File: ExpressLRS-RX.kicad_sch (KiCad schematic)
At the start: 34 parts, among them J2 Conn_Coaxial, U60 ESP8285H16, U61 Crystal_GND24, U70 SX1280, U71 Crystal_GND24

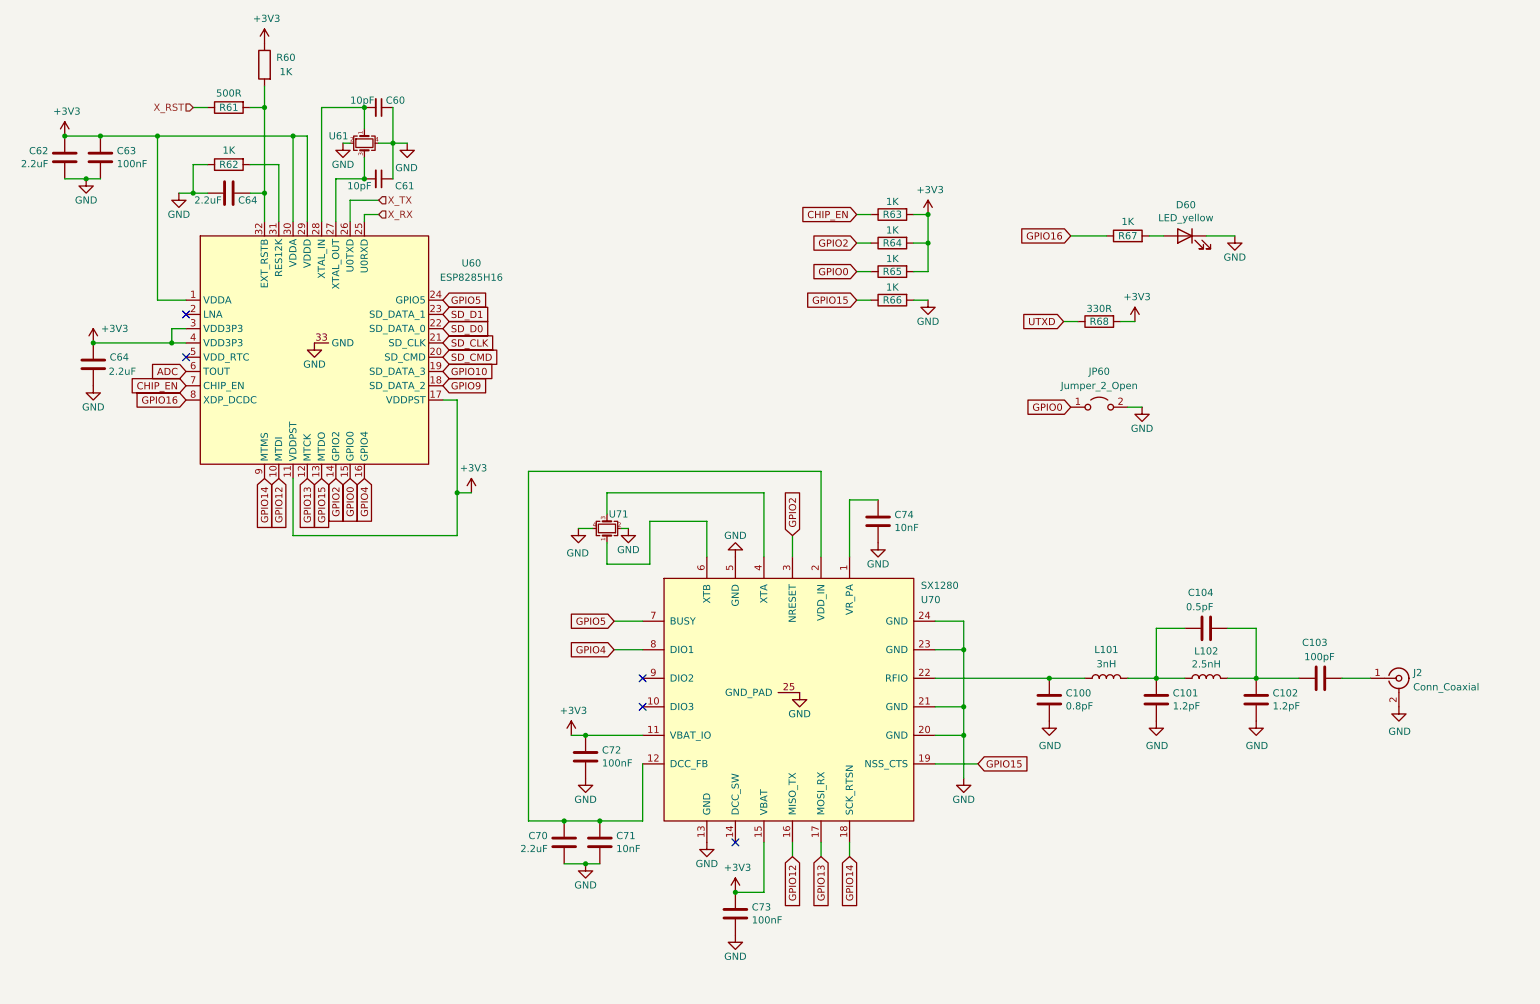
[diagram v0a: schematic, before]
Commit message: Initial board layout completed + initial routing started
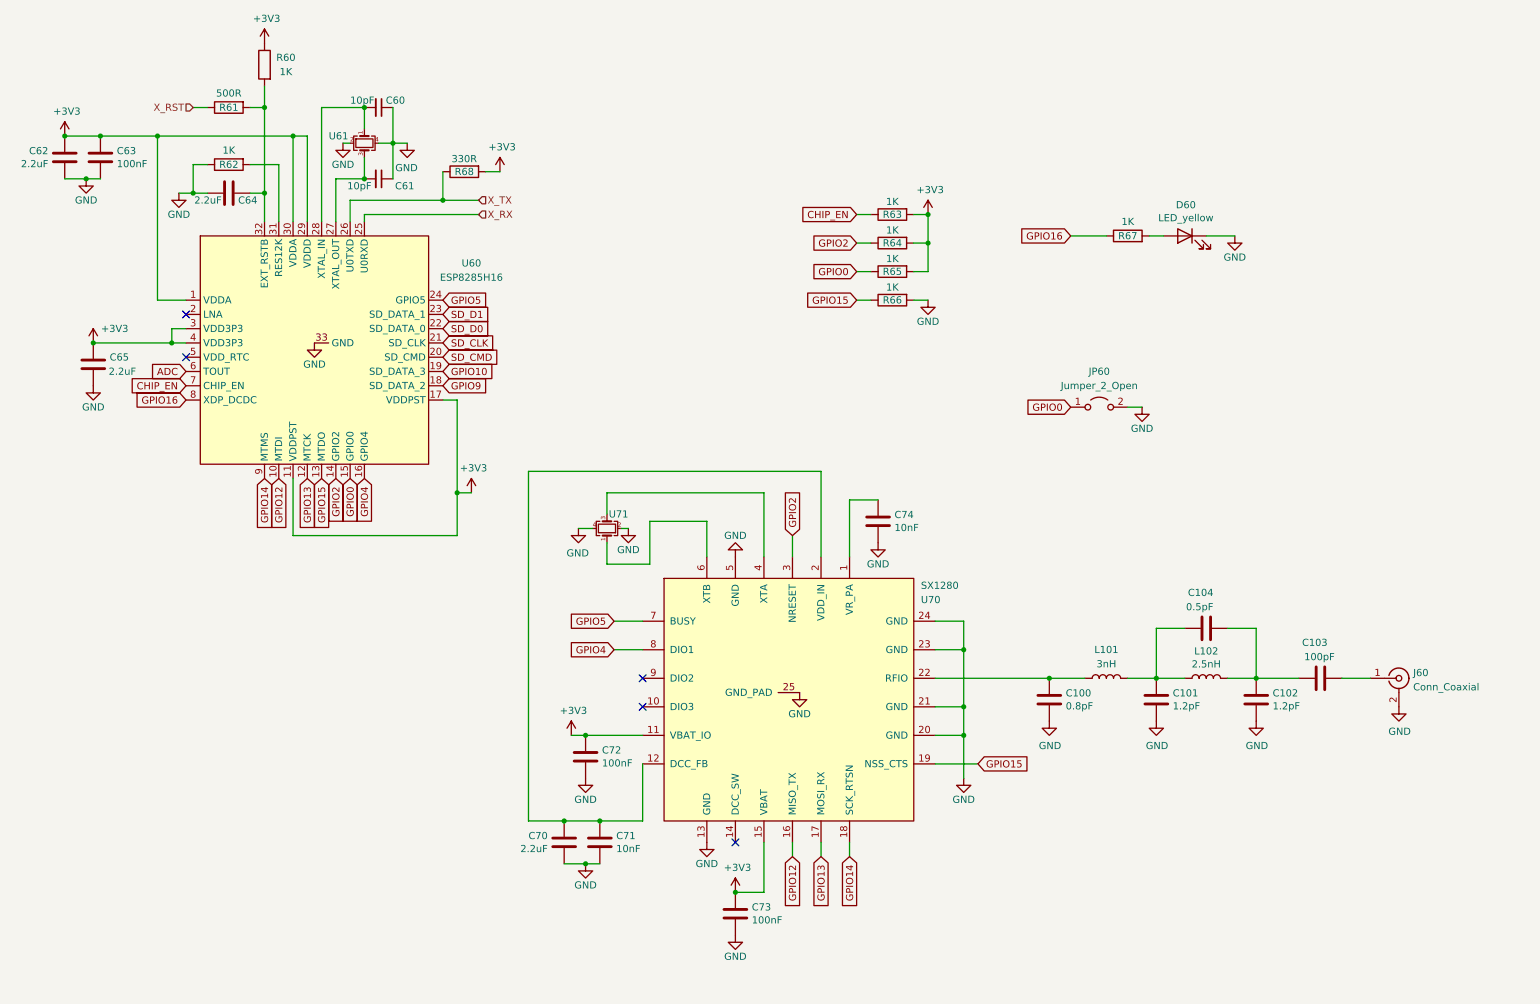
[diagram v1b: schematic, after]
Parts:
- U61: value Crystal_GND24 -> Crystal_ESP8285; footprint Crystal:Crystal_SMD_3225-4Pin_3.2x2.5mm -> Crystal:Crystal_SMD_2016-4Pin_2.0x1.6mm; LCSC C15192 -> C669081
- U71: value Crystal_GND24 -> Crystal_SX1280
- renumbered C64 to C65, J2 to J60
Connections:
- net UTXD is gone; now on net X_TX: R68.1
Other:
- moved on the sheet: R68
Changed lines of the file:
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@@
   (junction (at 143.51 173.99) (diameter 0) (color 0 0 0 0)
+  )
+  (junction (at 91.44 50.8) (diameter 0) (color 0 0 0 0)
   )
   (junction (at 77.47 46.99) (diameter 0) (color 0 0 0 0)
@@
     (stroke (width 0) (type default) (color 0 0 0 0))
   )
+  (wire (pts (xy 91.44 45.72) (xy 91.44 50.8))
+    (stroke (width 0) (type default) (color 0 0 0 0))
+  )
   (wire (pts (xy 106.68 161.29) (xy 113.03 161.29))
     (stroke (width 0) (type default) (color 0 0 0 0))
@@
     (stroke (width 0) (type default) (color 0 0 0 0))
   )
-  (wire (pts (xy 80.01 50.8) (xy 74.93 50.8))
+  (wire (pts (xy 97.79 50.8) (xy 91.44 50.8))
     (stroke (width 0) (type default) (color 0 0 0 0))
   )
@@
     (stroke (width 0) (type default) (color 0 0 0 0))
   )
-  (wire (pts (xy 212.09 72.39) (xy 214.63 72.39))
+  (wire (pts (xy 99.06 45.72) (xy 101.6 45.72))
     (stroke (width 0) (type default) (color 0 0 0 0))
   )
@@
     (stroke (width 0) (type default) (color 0 0 0 0))
   )
-  (wire (pts (xy 201.93 72.39) (xy 204.47 72.39))
-    (stroke (width 0) (type default) (color 0 0 0 0))
-  )
   (wire (pts (xy 106.68 161.29) (xy 106.68 99.06))
     (stroke (width 0) (type default) (color 0 0 0 0))
@@
     (stroke (width 0) (type default) (color 0 0 0 0))
   )
-  (wire (pts (xy 77.47 53.34) (xy 80.01 53.34))
+  (wire (pts (xy 77.47 53.34) (xy 97.79 53.34))
     (stroke (width 0) (type default) (color 0 0 0 0))
   )
@@
     (stroke (width 0) (type default) (color 0 0 0 0))
   )
+  (wire (pts (xy 91.44 50.8) (xy 74.93 50.8))
+    (stroke (width 0) (type default) (color 0 0 0 0))
+  )
   (wire (pts (xy 184.15 140.97) (xy 184.15 130.81))
     (stroke (width 0) (type default) (color 0 0 0 0))
@@
     (effects (font (size 1.27 1.27)) (justify right))
     (property "Intersheet References" "${INTERSHEET_REFS}" (id 0) (at 113.911 125.8094 0)
-      (effects (font (size 1.27 1.27)) (justify right) hide)
-    )
-  )
-  (global_label "UTXD" (shape input) (at 201.93 72.39 180) (fields_autoplaced)
-    (effects (font (size 1.27 1.27)) (justify right))
-    (property "Intersheet References" "${INTERSHEET_REFS}" (id 0) (at 194.8282 72.4694 0)
       (effects (font (size 1.27 1.27)) (justify right) hide)
     )
@@
     )
   )
-  (hierarchical_label "X_TX" (shape input) (at 80.01 50.8 0)
+  (hierarchical_label "X_TX" (shape input) (at 97.79 50.8 0)
     (effects (font (size 1.27 1.27)) (justify left))
   )
-  (hierarchical_label "X_RX" (shape input) (at 80.01 53.34 0)
+  (hierarchical_label "X_RX" (shape input) (at 97.79 53.34 0)
     (effects (font (size 1.27 1.27)) (justify left))
   )
@@
   (symbol (lib_id "power:GND") (at 73.66 40.64 0) (unit 1)
     (in_bom yes) (on_board yes)
-    (property "Reference" "#PWR0111" (id 0) (at 73.66 46.99 0)
+    (property "Reference" "#PWR0165" (id 0) (at 73.66 46.99 0)
       (effects (font (size 1.27 1.27)) hide)
     )
@@
   (symbol (lib_id "power:GND") (at 261.62 140.97 0) (unit 1)
     (in_bom yes) (on_board yes)
-    (property "Reference" "#PWR0126" (id 0) (at 261.62 147.32 0)
+    (property "Reference" "#PWR0169" (id 0) (at 261.62 147.32 0)
       (effects (font (size 1.27 1.27)) hide)
     )
@@
   (symbol (lib_id "power:GND") (at 68.58 76.2 0) (unit 1)
     (in_bom yes) (on_board yes)
-    (property "Reference" "#PWR0110" (id 0) (at 68.58 82.55 0)
+    (property "Reference" "#PWR0167" (id 0) (at 68.58 82.55 0)
       (effects (font (size 1.27 1.27)) hide)
     )
@@
     (pin "1")
   )
-  (symbol (lib_id "Device:R") (at 208.28 72.39 90) (mirror x) (unit 1)
-    (in_bom yes) (on_board yes)
-    (property "Reference" "R68" (id 0) (at 208.28 72.39 90))
-    (property "Value" "330R" (id 1) (at 208.28 70.104 90))
-    (property "Footprint" "Resistor_SMD:R_0402_1005Metric" (id 2) (at 208.28 70.612 90)
-      (effects (font (size 1.27 1.27)) hide)
-    )
-    (property "Datasheet" "?" (id 3) (at 208.28 72.39 0)
-      (effects (font (size 1.27 1.27)) hide)
-    )
-    (property "LCSC" "?" (id 4) (at 208.28 72.39 0)
+  (symbol (lib_id "Device:R") (at 95.25 45.72 90) (mirror x) (unit 1)
+    (in_bom yes) (on_board yes)
+    (property "Reference" "R68" (id 0) (at 95.25 45.72 90))
+    (property "Value" "330R" (id 1) (at 95.25 43.434 90))
+    (property "Footprint" "Resistor_SMD:R_0402_1005Metric" (id 2) (at 95.25 43.942 90)
+      (effects (font (size 1.27 1.27)) hide)
+    )
+    (property "Datasheet" "?" (id 3) (at 95.25 45.72 0)
+      (effects (font (size 1.27 1.27)) hide)
+    )
+    (property "LCSC" "?" (id 4) (at 95.25 45.72 0)
       (effects (font (size 1.27 1.27)) hide)
     )
@@
   (symbol (lib_id "power:+3V3") (at 29.21 76.2 0) (unit 1)
     (in_bom yes) (on_board yes)
-    (property "Reference" "#PWR0107" (id 0) (at 29.21 80.01 0)
+    (property "Reference" "#PWR0166" (id 0) (at 29.21 80.01 0)
       (effects (font (size 1.27 1.27)) hide)
     )
@@
   (symbol (lib_id "power:+3V3") (at 177.8 53.34 0) (unit 1)
     (in_bom yes) (on_board yes)
-    (property "Reference" "#PWR0103" (id 0) (at 177.8 57.15 0)
+    (property "Reference" "#PWR0168" (id 0) (at 177.8 57.15 0)
       (effects (font (size 1.27 1.27)) hide)
     )
@@
   (symbol (lib_id "Device:C") (at 29.21 80.01 0) (mirror y) (unit 1)
     (in_bom yes) (on_board yes)
-    (property "Reference" "C64" (id 0) (at 35.56 78.74 0)
+    (property "Reference" "C65" (id 0) (at 35.56 78.74 0)
       (effects (font (size 1.27 1.27)) (justify left))
     )
@@
   (symbol (lib_id "Connector:Conn_Coaxial") (at 261.62 135.89 0) (unit 1)
     (in_bom yes) (on_board yes) (fields_autoplaced)
-    (property "Reference" "J2" (id 0) (at 264.16 134.9131 0)
+    (property "Reference" "J60" (id 0) (at 264.16 134.9131 0)
       (effects (font (size 1.27 1.27)) (justify left))
     )
@@
     (pin "1")
   )
-  (symbol (lib_id "power:+3V3") (at 214.63 72.39 0) (unit 1)
-    (in_bom yes) (on_board yes)
-    (property "Reference" "#PWR0115" (id 0) (at 214.63 76.2 0)
-      (effects (font (size 1.27 1.27)) hide)
-    )
-    (property "Value" "+3V3" (id 1) (at 215.011 67.9958 0))
-    (property "Footprint" "" (id 2) (at 214.63 72.39 0)
-      (effects (font (size 1.27 1.27)) hide)
-    )
-    (property "Datasheet" "" (id 3) (at 214.63 72.39 0)
+  (symbol (lib_id "power:+3V3") (at 101.6 45.72 0) (unit 1)
+    (in_bom yes) (on_board yes)
+    (property "Reference" "#PWR0115" (id 0) (at 101.6 49.53 0)
+      (effects (font (size 1.27 1.27)) hide)
+    )
+    (property "Value" "+3V3" (id 1) (at 101.981 41.3258 0))
+    (property "Footprint" "" (id 2) (at 101.6 45.72 0)
+      (effects (font (size 1.27 1.27)) hide)
+    )
+    (property "Datasheet" "" (id 3) (at 101.6 45.72 0)
       (effects (font (size 1.27 1.27)) hide)
     )
@@
       (effects (font (size 1.27 1.27)) (justify left))
     )
-    (property "Value" "Crystal_GND24" (id 1) (at 123.19 107.95 0)
+    (property "Value" "Crystal_SX1280" (id 1) (at 123.19 107.95 0)
       (effects (font (size 1.27 1.27)) (justify left) hide)
     )
@@
       (effects (font (size 1.27 1.27)) (justify left))
     )
-    (property "Value" "Crystal_GND24" (id 1) (at 74.93 41.91 0)
+    (property "Value" "Crystal_ESP8285" (id 1) (at 74.93 41.91 0)
       (effects (font (size 1.27 1.27)) (justify left) hide)
     )
-    (property "Footprint" "Crystal:Crystal_SMD_3225-4Pin_3.2x2.5mm" (id 2) (at 77.47 40.64 0)
-      (effects (font (size 1.27 1.27)) hide)
-    )
-    (property "Datasheet" "https://lcsc.com/product-detail/Crystals_Yangxing-Tech-Yangxing-Tech-X322526MMB4SI_C15192.html" (id 3) (at 77.47 40.64 0)
-      (effects (font (size 1.27 1.27)) hide)
-    )
-    (property "LCSC" "C15192" (id 4) (at 77.47 40.64 0)
+    (property "Footprint" "Crystal:Crystal_SMD_2016-4Pin_2.0x1.6mm" (id 2) (at 77.47 40.64 0)
+      (effects (font (size 1.27 1.27)) hide)
+    )
+    (property "Datasheet" "https://lcsc.com/product-detail/Oscillators_Yangxing-Tech-Yangxing-Tech-OT201626MJBA4SL_C669081.html" (id 3) (at 77.47 40.64 0)
+      (effects (font (size 1.27 1.27)) hide)
+    )
+    (property "LCSC" "C669081" (id 4) (at 77.47 40.64 0)
       (effects (font (size 1.27 1.27)) hide)
     )
@@
   (symbol (lib_id "power:+3V3") (at 24.13 39.37 0) (unit 1)
     (in_bom yes) (on_board yes)
-    (property "Reference" "#PWR0106" (id 0) (at 24.13 43.18 0)
+    (property "Reference" "#PWR0171" (id 0) (at 24.13 43.18 0)
       (effects (font (size 1.27 1.27)) hide)
     )
@@
   (symbol (lib_id "power:GND") (at 27.94 46.99 0) (unit 1)
     (in_bom yes) (on_board yes)
-    (property "Reference" "#PWR0108" (id 0) (at 27.94 53.34 0)
+    (property "Reference" "#PWR0170" (id 0) (at 27.94 53.34 0)
       (effects (font (size 1.27 1.27)) hide)
     )
@@
   (symbol (lib_id "power:+3V3") (at 96.52 102.87 0) (unit 1)
     (in_bom yes) (on_board yes)
-    (property "Reference" "#PWR0109" (id 0) (at 96.52 106.68 0)
-      (effects (font (size 1.27 1.27)) hide)
-    )
+    (property "Reference" "#PWR0172" (id 0) (at 96.52 106.68 0)
+      (effects (font (size 1.27 1.27)) hide)
+    )

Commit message: All LCSC components selected
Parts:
- removed R61: 500R, Resistor_SMD:R_0402_1005Metric, symbol Device:R
- C100: LCSC ? -> C115605
- C101, C102: LCSC ? -> C115613
- C103: LCSC ? -> C1546
- C104: LCSC ? -> C147327
- C60, C61: LCSC ? -> C32949
- C62, C64, C65, C70: LCSC ? -> C12530
- C71, C74: LCSC ? -> C15195
- R60, R62, R63, R64, R65, R66, R67: LCSC ? -> C11702
- R68: LCSC ? -> C25104
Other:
- moved on the sheet: R60

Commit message: fixed 26MHz XO and 12KRES resistor
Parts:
- R60: value 1K -> 12K; LCSC C11702 -> (none)
- U61: LCSC C669081 -> C390789
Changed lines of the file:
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@@
     (in_bom yes) (on_board yes)
     (property "Reference" "R60" (id 0) (at 63.5 30.48 0))
-    (property "Value" "1K" (id 1) (at 63.5 33.02 0))
+    (property "Value" "12K" (id 1) (at 63.5 33.02 0))
     (property "Footprint" "Resistor_SMD:R_0402_1005Metric" (id 2) (at 61.468 31.75 90)
       (effects (font (size 1.27 1.27)) hide)
     )
-    (property "Datasheet" "https://lcsc.com/product-detail/Chip-Resistor---Surface-Mount_UNI-ROYALUniroyal-Elec-UNI-ROYALUniroyal-Elec-0402WGF1001TCE_C11702.html" (id 3) (at 59.69 31.75 0)
+    (property "Datasheet" "" (id 3) (at 59.69 31.75 0)
       (effects (font (size 1.27 1.27)) hide)
     )
-    (property "LCSC" "C11702" (id 4) (at 59.69 31.75 0)
+    (property "LCSC" "" (id 4) (at 59.69 31.75 0)
       (effects (font (size 1.27 1.27)) hide)
     )
@@
       (effects (font (size 1.27 1.27)) hide)
     )
-    (property "Datasheet" "https://lcsc.com/product-detail/Oscillators_Yangxing-Tech-Yangxing-Tech-OT201626MJBA4SL_C669081.html" (id 3) (at 77.47 40.64 0)
+    (property "Datasheet" "https://www.lcsc.com/product-detail/Crystals_JGHC-JGHC-S2126000121080_C390789.html" (id 3) (at 77.47 40.64 0)
       (effects (font (size 1.27 1.27)) hide)
     )
-    (property "LCSC" "C669081" (id 4) (at 77.47 40.64 0)
+    (property "LCSC" "C390789" (id 4) (at 77.47 40.64 0)
       (effects (font (size 1.27 1.27)) hide)
     )

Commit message: Hardware bought of Rotini V2
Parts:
- added J61: Conn_01x01_Female, AlfredoFootprints:TGD-antenna-THT, symbol Connector:Conn_01x01_Female
- R60: LCSC (none) -> C25752
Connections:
- net at C103.2, J60.1 (In): now also J61.1 (Pin_1)
- net trace_antenna: now reaches U60.2 (LNA)
- no-connect marks 5 -> 4
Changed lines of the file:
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@@
   (junction (at 218.44 135.89) (diameter 0) (color 0 0 0 0)
+  )
+  (junction (at 254 135.89) (diameter 0) (color 0 0 0 0)
   )
   (junction (at 184.15 140.97) (diameter 0) (color 0 0 0 0)
@@
   (no_connect (at 127 140.97))
   (no_connect (at 127 135.89))
-  (no_connect (at 45.72 71.12))
   (wire (pts (xy 148.59 114.3) (xy 148.59 102.87))
     (stroke (width 0) (type default) (color 0 0 0 0))
@@
     (stroke (width 0) (type default) (color 0 0 0 0))
   )
+  (wire (pts (xy 254 135.89) (xy 256.54 135.89))
+    (stroke (width 0) (type default) (color 0 0 0 0))
+  )
   (wire (pts (xy 179.07 140.97) (xy 184.15 140.97))
     (stroke (width 0) (type default) (color 0 0 0 0))
@@
     (stroke (width 0) (type default) (color 0 0 0 0))
   )
+  (wire (pts (xy 30.48 71.12) (xy 45.72 71.12))
+    (stroke (width 0) (type default) (color 0 0 0 0))
+  )
   (wire (pts (xy 138.43 107.95) (xy 138.43 114.3))
     (stroke (width 0) (type default) (color 0 0 0 0))
@@
     (stroke (width 0) (type default) (color 0 0 0 0))
   )
+  (wire (pts (xy 254 128.27) (xy 256.54 128.27))
+    (stroke (width 0) (type default) (color 0 0 0 0))
+  )
   (wire (pts (xy 158.75 99.06) (xy 158.75 114.3))
     (stroke (width 0) (type default) (color 0 0 0 0))
@@
     (stroke (width 0) (type default) (color 0 0 0 0))
   )
-  (wire (pts (xy 251.46 135.89) (xy 256.54 135.89))
-    (stroke (width 0) (type default) (color 0 0 0 0))
-  )
   (wire (pts (xy 120.65 106.68) (xy 120.65 102.87))
     (stroke (width 0) (type default) (color 0 0 0 0))
@@
     (stroke (width 0) (type default) (color 0 0 0 0))
   )
+  (wire (pts (xy 251.46 135.89) (xy 254 135.89))
+    (stroke (width 0) (type default) (color 0 0 0 0))
+  )
   (wire (pts (xy 93.98 102.87) (xy 93.98 86.36))
     (stroke (width 0) (type default) (color 0 0 0 0))
@@
     (stroke (width 0) (type default) (color 0 0 0 0))
   )
+  (wire (pts (xy 254 135.89) (xy 254 128.27))
+    (stroke (width 0) (type default) (color 0 0 0 0))
+  )
   (wire (pts (xy 175.26 68.58) (xy 177.8 68.58))
     (stroke (width 0) (type default) (color 0 0 0 0))
@@
   (wire (pts (xy 165.1 58.42) (xy 167.64 58.42))
     (stroke (width 0) (type default) (color 0 0 0 0))
+  )
+  (label "trace_antenna" (at 31.75 71.12 0)
+    (effects (font (size 1.27 1.27)) (justify left bottom))
   )
   (global_label "GPIO5" (shape input) (at 121.92 125.73 180) (fields_autoplaced)
@@
       (effects (font (size 1.27 1.27)) hide)
     )
-    (property "Datasheet" "" (id 3) (at 59.69 31.75 0)
-      (effects (font (size 1.27 1.27)) hide)
-    )
-    (property "LCSC" "" (id 4) (at 59.69 31.75 0)
+    (property "Datasheet" "https://www.lcsc.com/product-detail/Chip-Resistor---Surface-Mount_UNI-ROYALUniroyal-Elec-UNI-ROYALUniroyal-Elec-0402WGF1202TCE_C25752.html" (id 3) (at 59.69 31.75 0)
+      (effects (font (size 1.27 1.27)) hide)
+    )
+    (property "LCSC" "C25752" (id 4) (at 59.69 31.75 0)
       (effects (font (size 1.27 1.27)) hide)
     )
@@
     (pin "2")
   )
+  (symbol (lib_id "Connector:Conn_01x01_Female") (at 261.62 128.27 0) (unit 1)
+    (in_bom yes) (on_board yes)
+    (property "Reference" "J61" (id 0) (at 264.16 125.73 0)
+      (effects (font (size 1.27 1.27)) (justify left))
+    )
+    (property "Value" "Conn_01x01_Female" (id 1) (at 262.89 128.27 0)
+      (effects (font (size 1.27 1.27)) (justify left))
+    )
+    (property "Footprint" "AlfredoFootprints:TGD-antenna-THT" (id 2) (at 261.62 128.27 0)
+      (effects (font (size 1.27 1.27)) hide)
+    )
+    (property "Datasheet" "~" (id 3) (at 261.62 128.27 0)
+      (effects (font (size 1.27 1.27)) hide)
+    )
+    (property "LCSC" "~" (id 4) (at 261.62 128.27 0)
+      (effects (font (size 1.27 1.27)) hide)
+    )
+    (pin "1")
+  )
   (symbol (lib_id "Device:R") (at 171.45 58.42 90) (mirror x) (unit 1)
